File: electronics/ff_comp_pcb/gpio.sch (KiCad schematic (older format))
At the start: 26 parts, among them J1 Micro_SD_Card_Det_Hirose_DM3AT, U2 A33, Y1 24Mhz, Y2 32.768khz

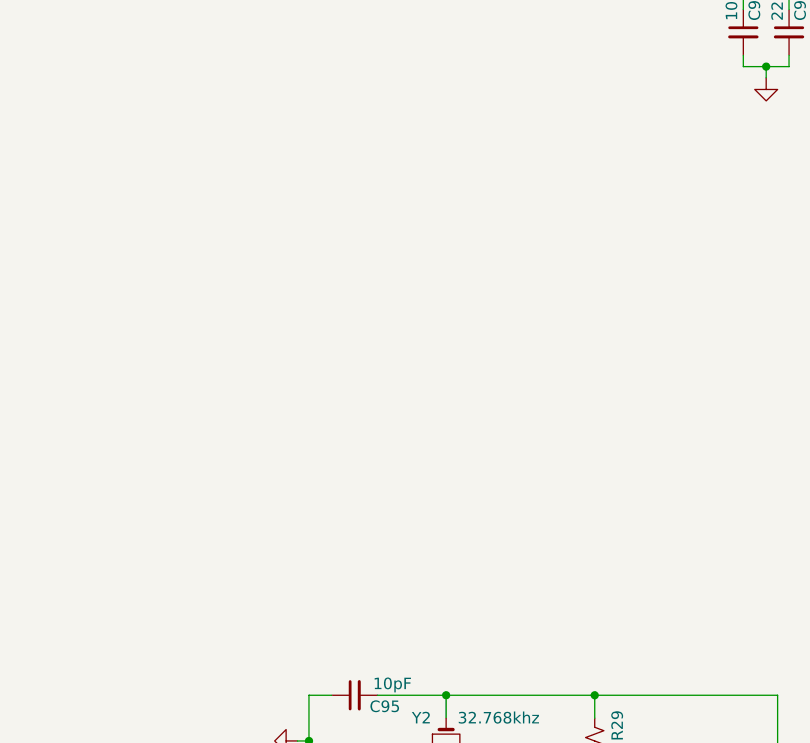
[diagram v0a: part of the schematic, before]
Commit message: Added the model for the usb, added a USB mux
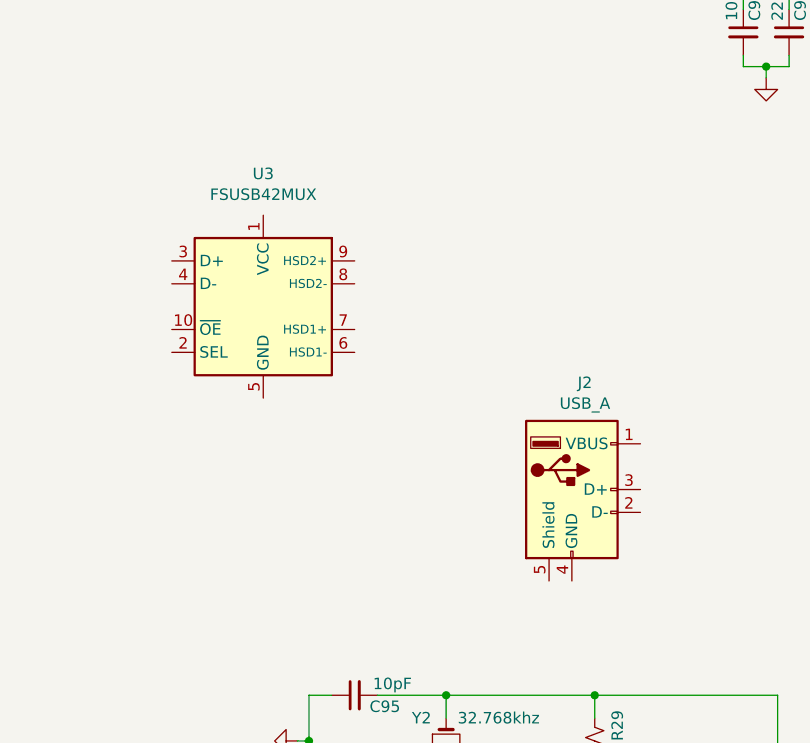
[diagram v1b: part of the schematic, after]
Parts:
- added J2: USB_A, Connector_USB:USB_A_Molex_67643_Horizontal, symbol Connector:USB_A
- added U3: FSUSB42MUX, Package_SO:MSOP-10_3x3mm_P0.5mm, symbol Interface_USB:FSUSB42MUX
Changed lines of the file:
@@
 Connection ~ 10750 5950
 Connection ~ 9800 5850
+$Comp
+L Connector:USB_A J2
+U 1 1 60B28733
+P 6750 3300
+F 0 "J2" H 6807 3767 50  0000 C CNN
+F 1 "USB_A" H 6807 3676 50  0000 C CNN
+F 2 "Connector_USB:USB_A_Molex_67643_Horizontal" H 6900 3250 50  0001 C CNN
+F 3 " ~" H 6900 3250 50  0001 C CNN
+F 4 "676430910" H 6750 3300 50  0001 C CNN "MPN"
+	1    6750 3300
+	1    0    0    -1
+$EndComp
+$Comp
+L Interface_USB:FSUSB42MUX U3
+U 1 1 60B2B3B3
+P 5400 2500
+F 0 "U3" H 5400 3081 50  0000 C CNN
+F 1 "FSUSB42MUX" H 5400 2990 50  0000 C CNN
+F 2 "Package_SO:MSOP-10_3x3mm_P0.5mm" H 5400 1700 50  0001 C CNN
+F 3 "https://www.onsemi.com/pub/Collateral/FSUSB42-D.PDF" H 5400 2400 50  0001 C CNN
+F 4 "FSUSB42MUX" H 5400 2500 50  0001 C CNN "MPN"
+	1    5400 2500
+	1    0    0    -1
+$EndComp
 $EndSCHEMATC

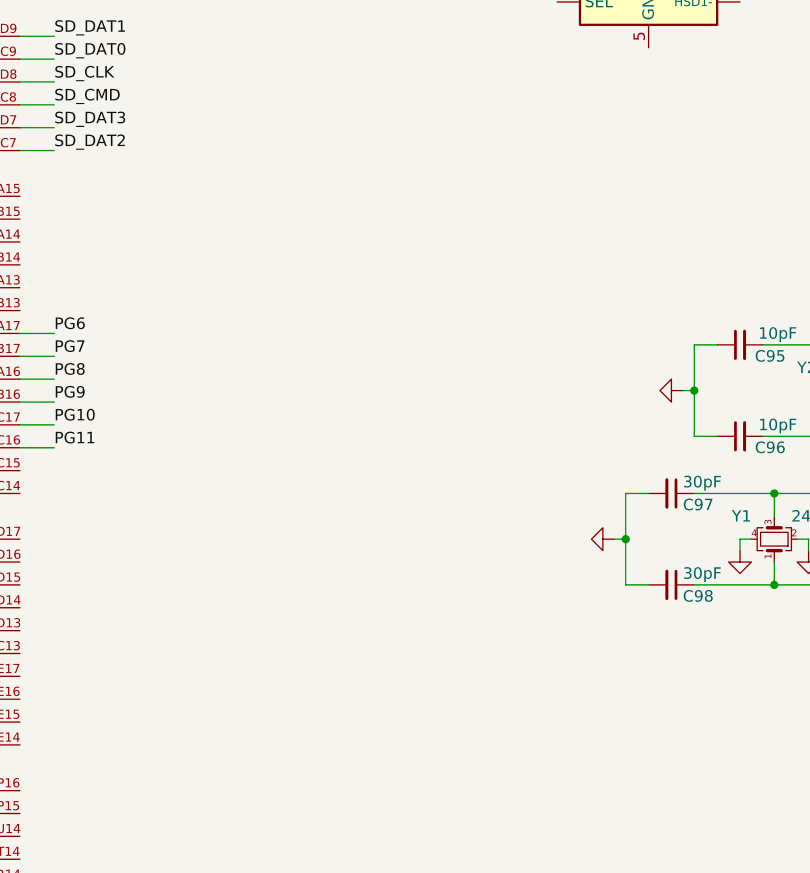
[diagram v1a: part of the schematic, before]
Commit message: Added the realtek wifi modules
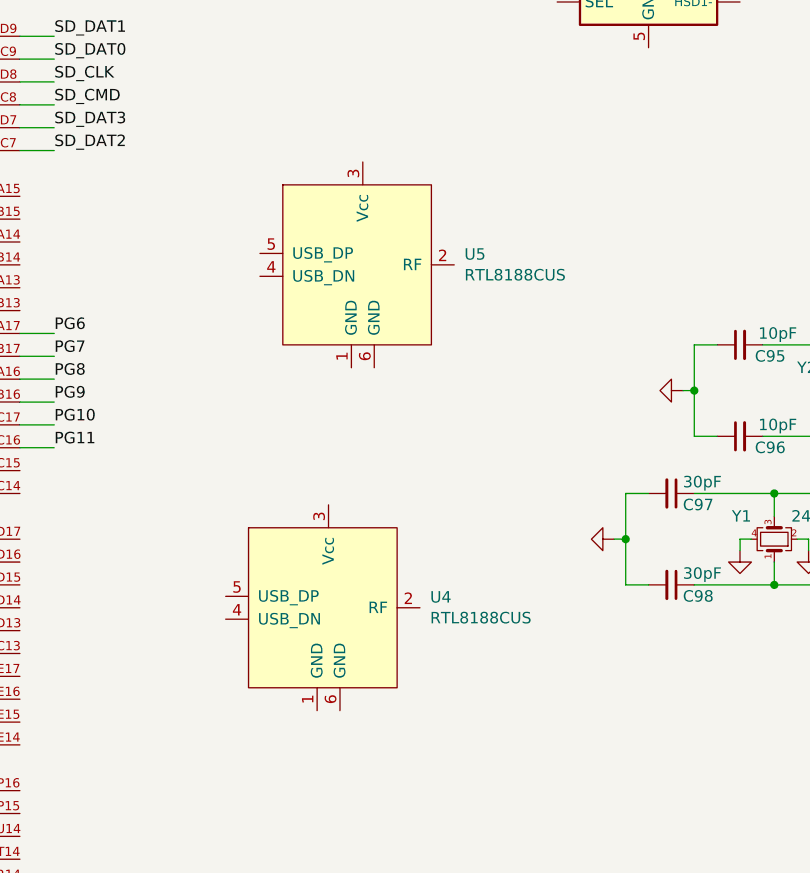
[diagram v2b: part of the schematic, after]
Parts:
- added U4, U5: RTL8188CUS, realtek:RTL8188CUS, symbol realtek:RTL8188CUS
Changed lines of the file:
@@
+	1    0    0    -1
+$EndComp
+$Comp
+L realtek:RTL8188CUS U5
+U 1 1 60B62A94
+P 4150 3850
+F 0 "U5" H 4594 3896 50  0000 L CNN
+F 1 "RTL8188CUS" H 4594 3805 50  0000 L CNN
+F 2 "realtek:RTL8188CUS" H 4650 3450 50  0001 C CNN
+F 3 "" H 3350 3900 50  0001 C CNN
+	1    4150 3850
+	1    0    0    -1
+$EndComp
+$Comp
+L realtek:RTL8188CUS U4
+U 1 1 60B6A2D9
+P 4000 5350
+F 0 "U4" H 4444 5396 50  0000 L CNN
+F 1 "RTL8188CUS" H 4444 5305 50  0000 L CNN
+F 2 "realtek:RTL8188CUS" H 4500 4950 50  0001 C CNN
+F 3 "" H 3200 5400 50  0001 C CNN
+	1    4000 5350
 	1    0    0    -1
 $EndComp

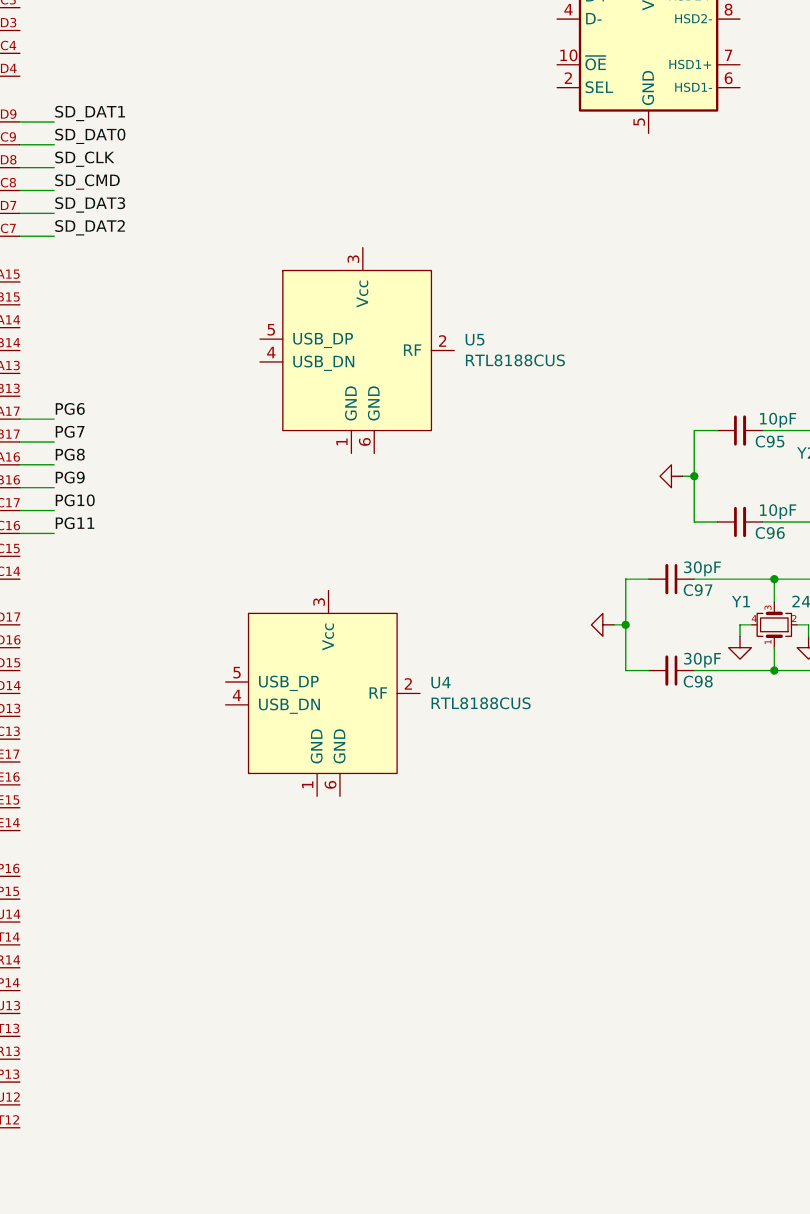
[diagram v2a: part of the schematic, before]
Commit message: Added the step file of the board to the model, added a u.fl connector in.
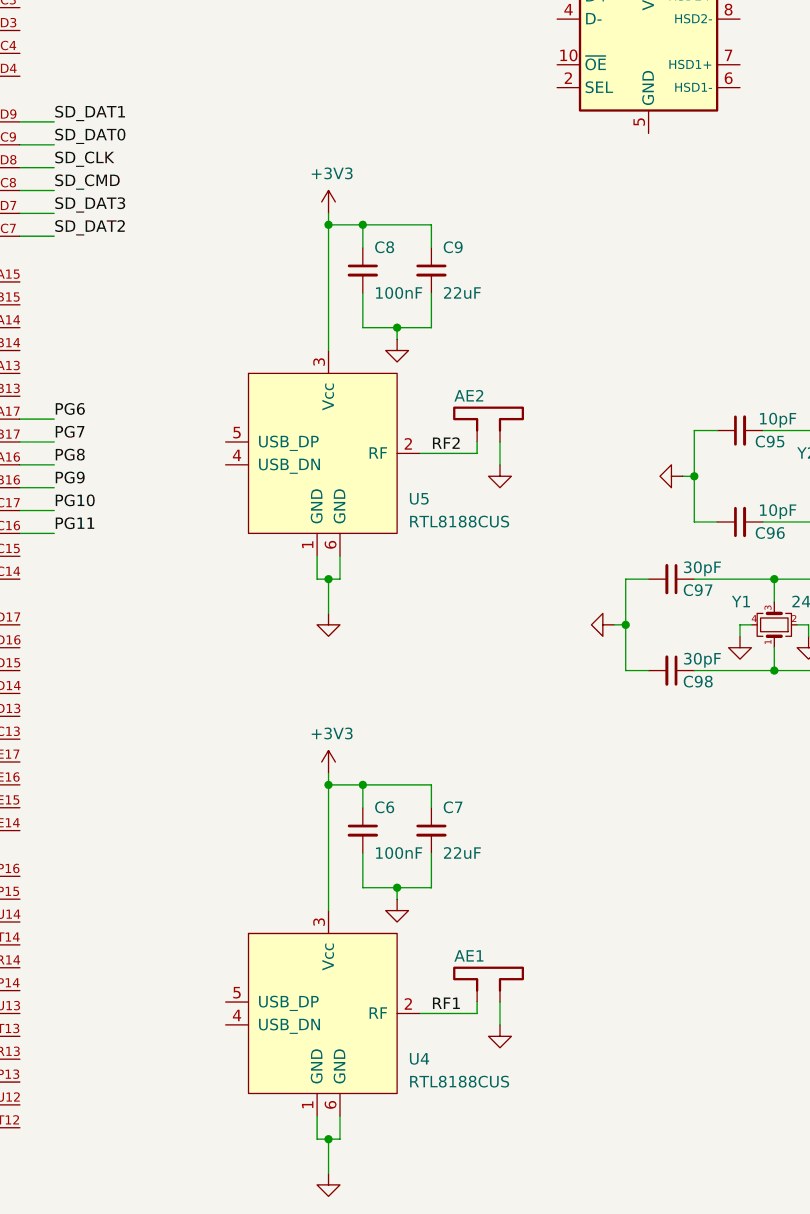
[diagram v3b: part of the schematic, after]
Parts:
- added AE1, AE2: Antenna_Dipole, Connector_Coaxial:U.FL_Hirose_U.FL-R-SMT-1_Vertical, symbol Device:Antenna_Dipole
- added C6, C8: 100nF, Capacitor_SMD:C_0402_1005Metric, symbol Device:C_Small
- added C7, C9: 22uF, Capacitor_SMD:C_0402_1005Metric, symbol Device:C_Small
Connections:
- net +3V3: now also U4.3 (Vcc), U5.3 (Vcc), C6.1, C7.1, C8.1, C9.1
- net GND: now also U4.1 (GND), U4.6 (GND), U5.1 (GND), U5.6 (GND), AE1.2, AE2.2, C6.2, C7.2, C8.2, C9.2
- net RF2: now reaches U5.2 (RF)
- net RF2: now also AE2.1
- net RF1: now reaches U4.2 (RF)
- net RF1: now also AE1.1
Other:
- moved on the sheet: U4, U5

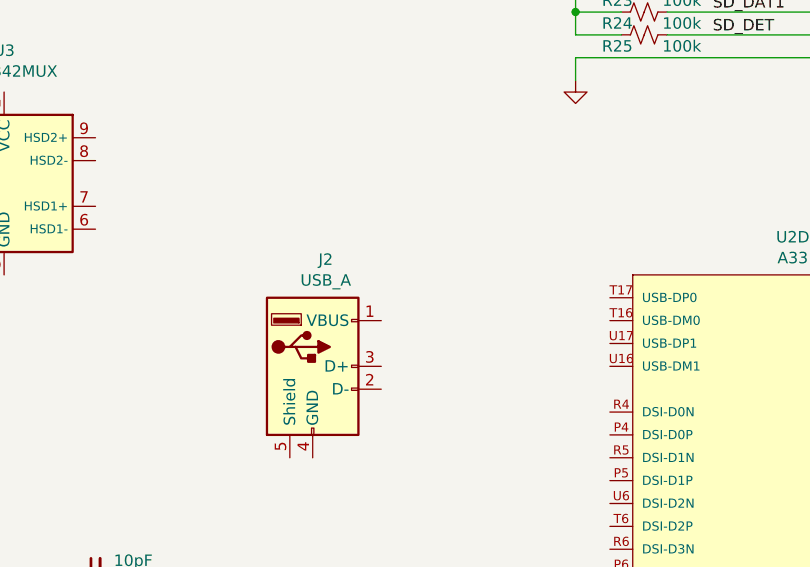
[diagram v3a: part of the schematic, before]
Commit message: Dropped down the board to board.
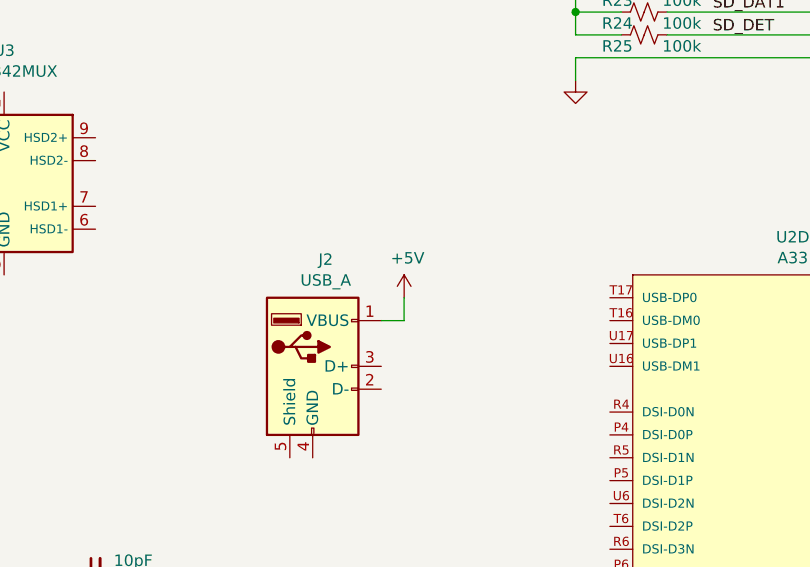
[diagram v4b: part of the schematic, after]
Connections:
- net +5V: now reaches J2.1 (VBUS)
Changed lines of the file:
@@
 Text Label 4450 4300 0    50   ~ 0
 RF2
+$Comp
+L power:+5V #PWR?
+U 1 1 614136E4
+P 7150 3000
+AR Path="/614136E4" Ref="#PWR?"  Part="1"
+AR Path="/6063BE69/614136E4" Ref="#PWR?"  Part="1"
+F 0 "#PWR?" H 7150 2850 50  0001 C CNN
+F 1 "+5V" H 7165 3173 50  0000 C CNN
+F 2 "" H 7150 3000 50  0001 C CNN
+F 3 "" H 7150 3000 50  0001 C CNN
+	1    7150 3000
+	1    0    0    -1
+$EndComp
+Wire Wire Line
+	7150 3000 7150 3100
+Wire Wire Line
+	7150 3100 7050 3100
 $EndSCHEMATC

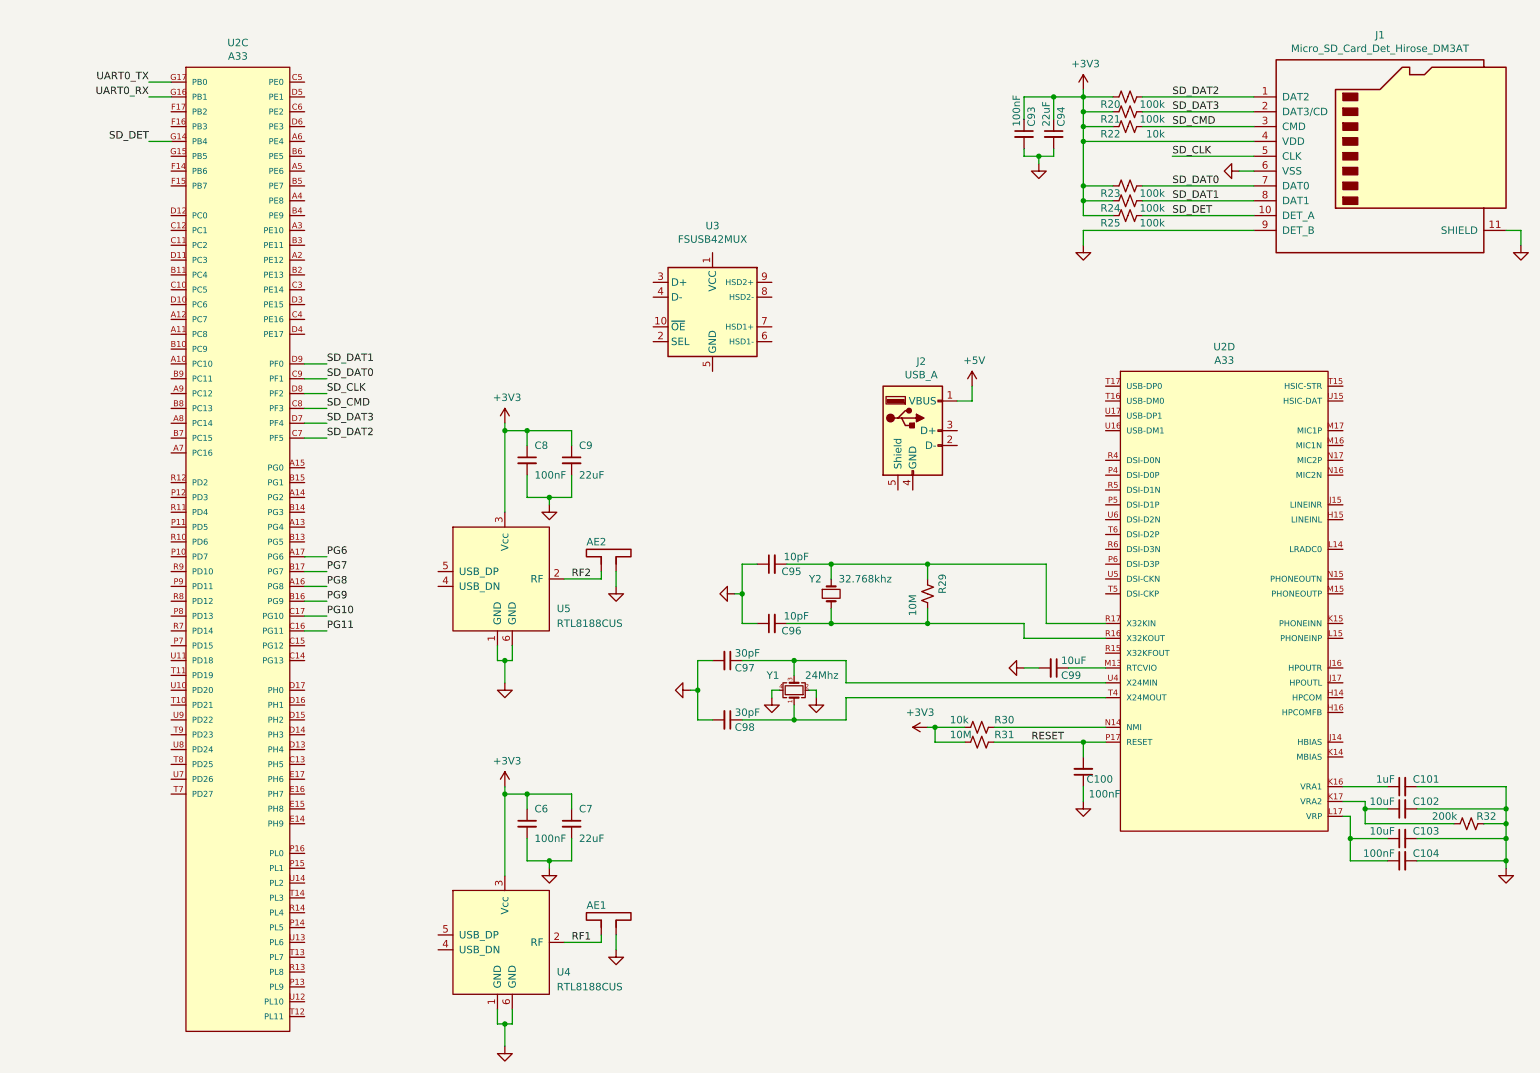
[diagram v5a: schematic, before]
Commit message: Finished up the routing on the power board, still needs a double check.
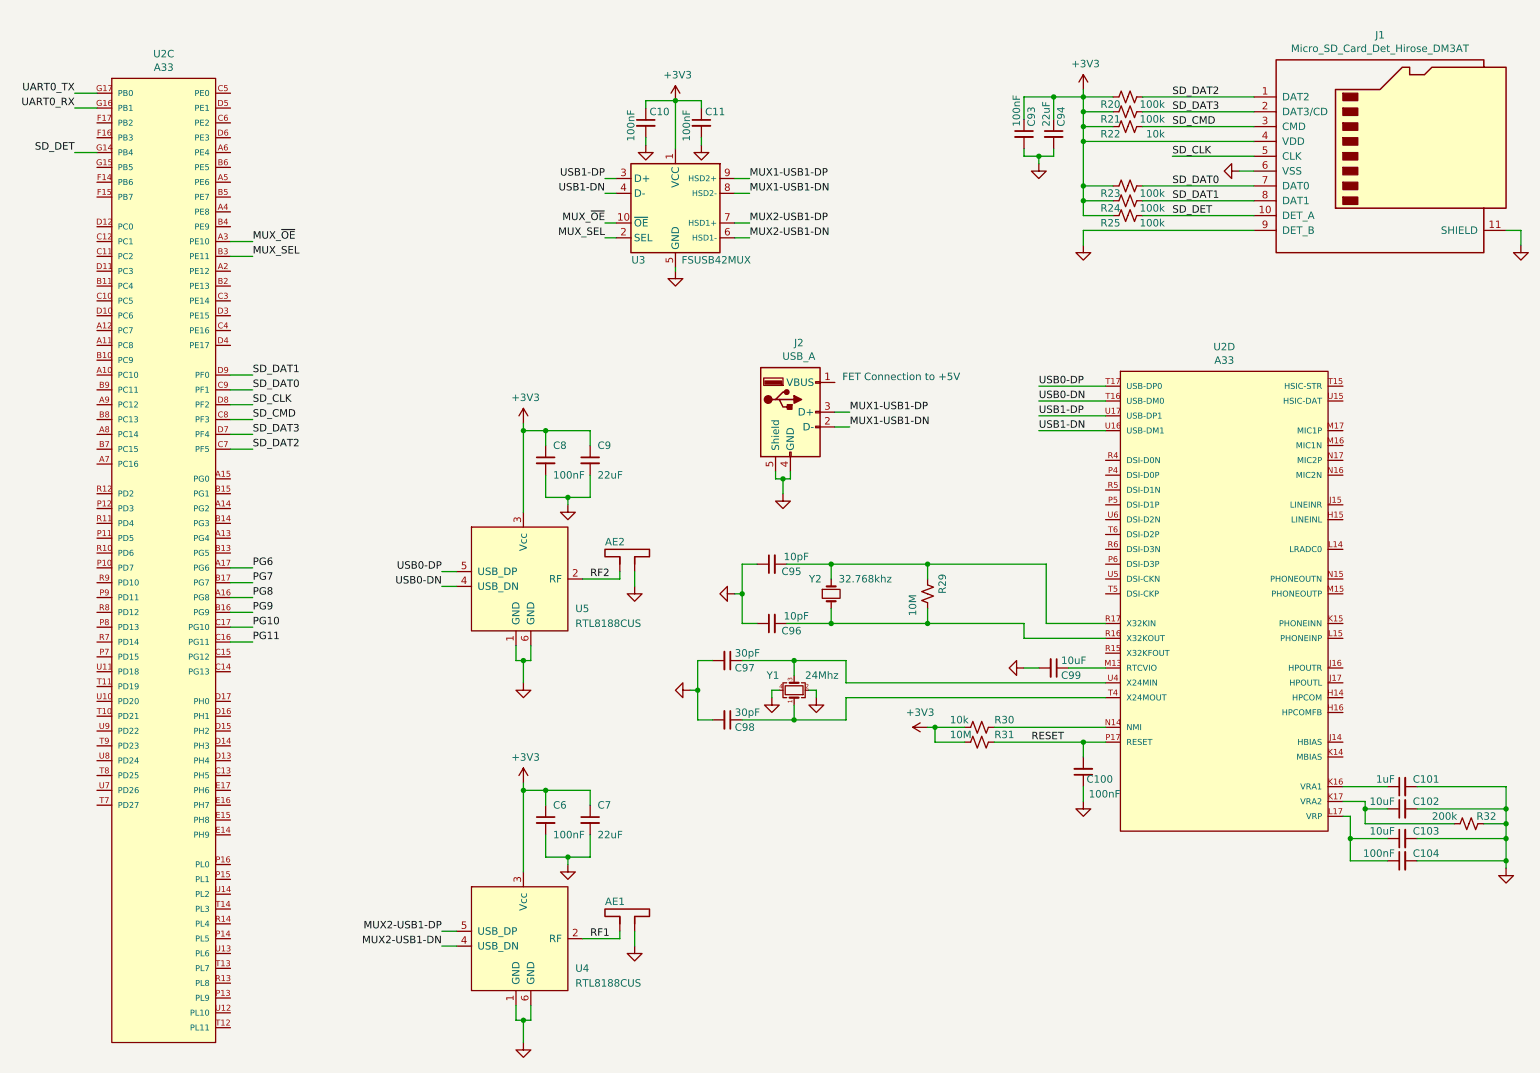
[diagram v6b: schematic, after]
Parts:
- added C10, C11: 100nF, Capacitor_SMD:C_0402_1005Metric, symbol Device:C_Small
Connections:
- net +3V3: now also U3.1 (VCC), C10.1, C11.1
- net GND: now also J2.4 (GND), J2.5 (Shield), U3.5 (GND), C10.2, C11.2
- net MUX_~OE: now reaches U2.A3 (PE10)
- net MUX_~OE: now also U3.10 (~OE)
- net MUX_SEL: now reaches U2.B3 (PE11)
- net MUX_SEL: now also U3.2 (SEL)
- net USB0-DN: now reaches U2.T16 (USB-DM0)
- net USB0-DN: now also U5.4 (USB_DN)
- net USB0-DP: now reaches U2.T17 (USB-DP0)
- net USB0-DP: now also U5.5 (USB_DP)
- net USB1-DN: now reaches U2.U16 (USB-DM1)
- net USB1-DN: now also U3.4 (D-)
- net USB1-DP: now reaches U2.U17 (USB-DP1)
- net USB1-DP: now also U3.3 (D+)
- net MUX1-USB1-DN: now reaches J2.2 (D-)
- net MUX1-USB1-DN: now also U3.8 (HSD2-)
- net MUX1-USB1-DP: now reaches J2.3 (D+)
- net MUX1-USB1-DP: now also U3.9 (HSD2+)
- net MUX2-USB1-DN: now reaches U3.6 (HSD1-)
- net MUX2-USB1-DN: now also U4.4 (USB_DN)
- net MUX2-USB1-DP: now reaches U3.7 (HSD1+)
- net MUX2-USB1-DP: now also U4.5 (USB_DP)
- net +5V: no longer names the net of J2.1 (VBUS)
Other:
- note added: "FET Connection to +5V"
- moved on the sheet: AE1, AE2, C6, C7, C8, C9, J2, U2C, U3, U4, U5
